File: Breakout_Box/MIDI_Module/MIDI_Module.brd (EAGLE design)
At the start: 55 x 80 mm, 71 parts, among them T1 2N2222, T2 2N2222, U1 LMV324, U2 LMV324, U3 MIC5205-5.0YM5-TR, U4 MIC5205-3.3YM5-TR

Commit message: Licenses
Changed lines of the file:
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@@
 <board>
 <plain>
-<wire x1="0" y1="0" x2="55" y2="0" width="0" layer="20"/>
-<wire x1="55" y1="0" x2="55" y2="80" width="0" layer="20"/>
-<wire x1="55" y1="80" x2="0" y2="80" width="0" layer="20"/>
-<wire x1="0" y1="80" x2="0" y2="0" width="0" layer="20"/>
+<wire x1="0" y1="0" x2="55" y2="0" width="0.1" layer="20"/>
+<wire x1="55" y1="0" x2="55" y2="80" width="0.1" layer="20"/>
+<wire x1="55" y1="80" x2="0" y2="80" width="0.1" layer="20"/>
+<wire x1="0" y1="80" x2="0" y2="0" width="0.1" layer="20"/>
 <text x="7.62" y="43.4975" size="0.8128" layer="25" ratio="13">CH9_CV</text>
 <text x="7.62" y="40.9575" size="0.8128" layer="25" ratio="13">CH10_CV</text>

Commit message: reset devel
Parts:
- U1, U2: value LMV324 -> TLV6004

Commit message: merge version_1.1 to devel
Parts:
- U1, U2: value TLV6004 -> LMV324

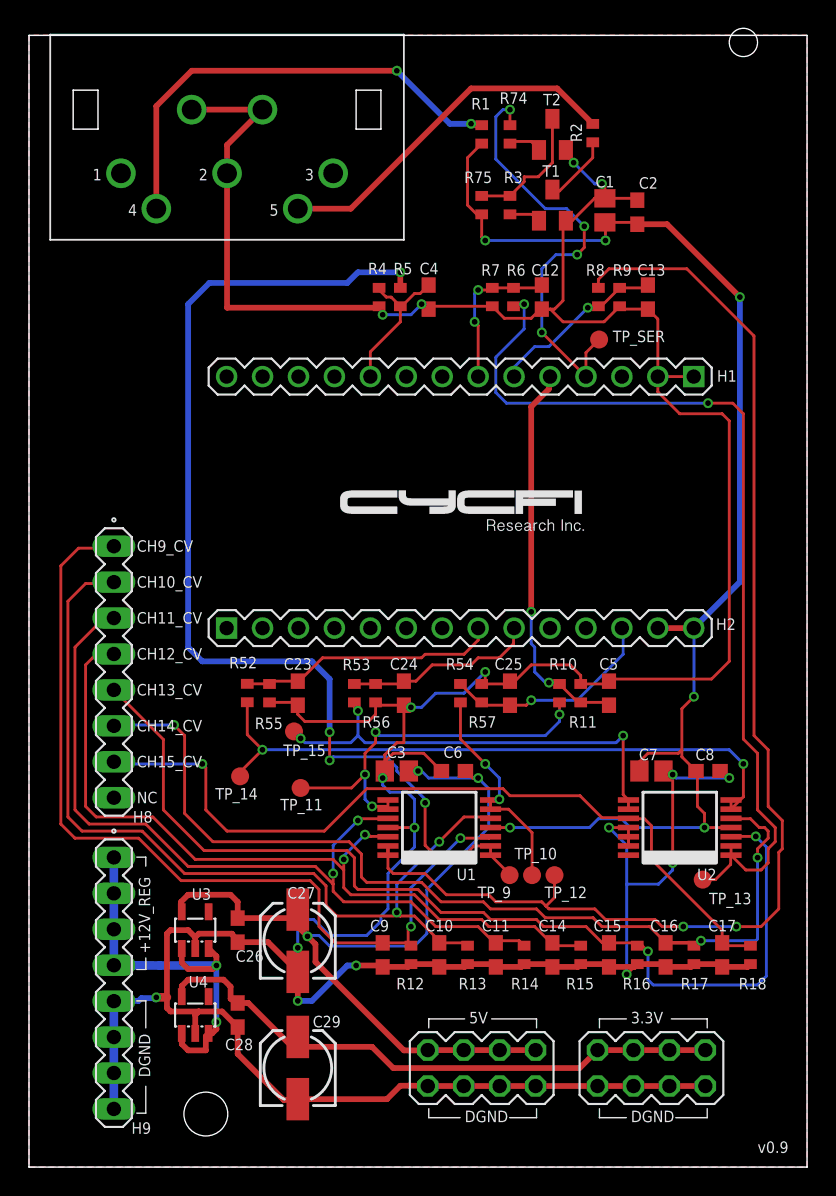
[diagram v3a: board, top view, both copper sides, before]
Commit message: create version 2.1 and update main and midi modules and delete nexyus cad drawings
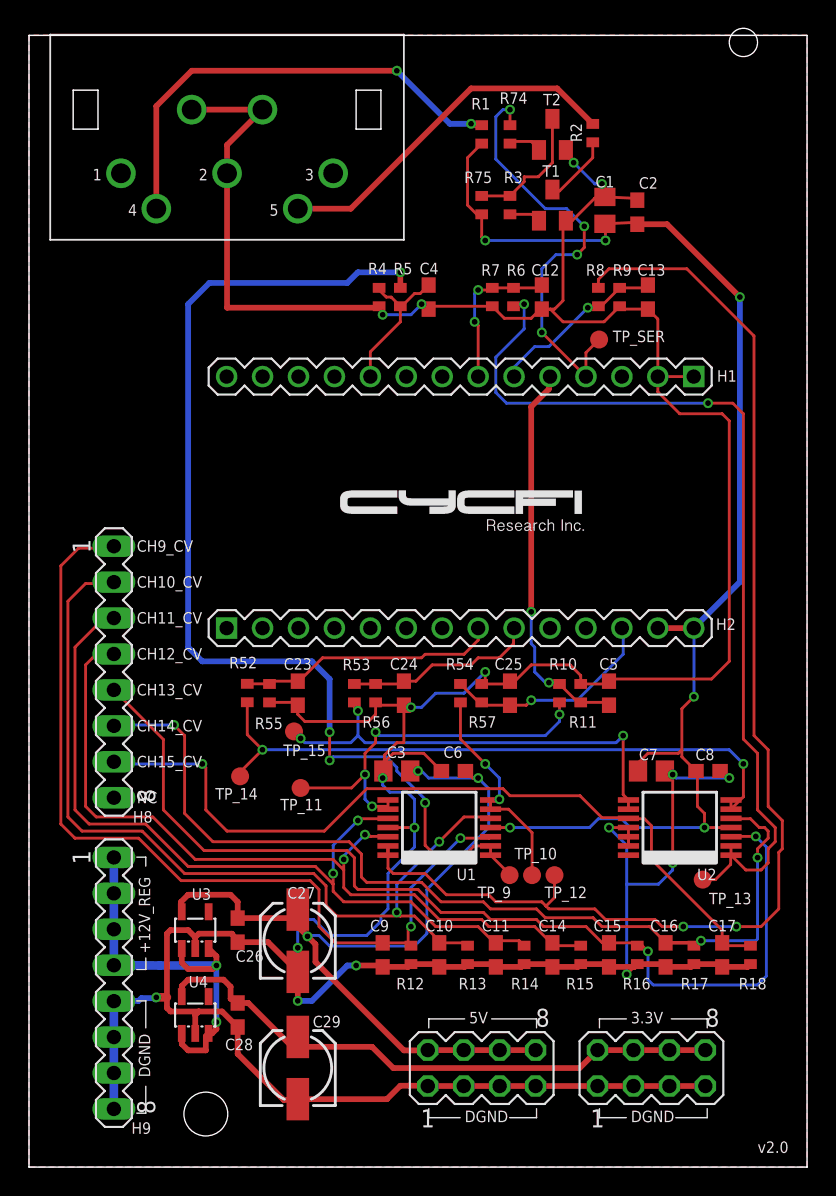
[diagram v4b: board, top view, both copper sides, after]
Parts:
- U1, U2: value LMV324 -> TLV6004
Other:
- board text added: "v2.0"
- board text removed: "v0.9"

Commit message: Slight Changes to MIDI and MCU: - Change BJT Part number on MIDI_Module - Delete Ferrite Bead on MCU_Module
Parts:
- T1, T2: value 2N2222 -> MMBT2222LT1G
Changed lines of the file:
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@@
 </autorouter>
 <elements>
-<element name="T1" library="Cycfi" package="SOT23-3" value="2N2222" x="37" y="68" smashed="yes">
+<element name="T1" library="Cycfi" package="SOT23-3" value="MMBT2222LT1G" x="37" y="68" smashed="yes">
 <attribute name="NAME" x="36.295" y="70.005" size="0.8128" layer="25" ratio="13"/>
 <attribute name="VALUE" x="35.095" y="64.825" size="0.8128" layer="27" ratio="13"/>
@@
 <attribute name="VALUE" x="24.468" y="34.389" size="0.8128" layer="27" ratio="13" rot="R270"/>
 </element>
-<element name="T2" library="Cycfi" package="SOT23-3" value="2N2222" x="37" y="73" smashed="yes">
+<element name="T2" library="Cycfi" package="SOT23-3" value="MMBT2222LT1G" x="37" y="73" smashed="yes">
 <attribute name="NAME" x="36.345" y="75.055" size="0.8128" layer="25" ratio="13"/>
 <attribute name="VALUE" x="35.095" y="69.825" size="0.8128" layer="27" ratio="13"/>
